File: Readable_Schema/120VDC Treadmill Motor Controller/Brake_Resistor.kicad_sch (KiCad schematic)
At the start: 13 parts, among them J7 TB005-762-02BE, Q9 IPP200N25N3GXKSA1, U10 FOD3182, U11 TC75S56F_LF

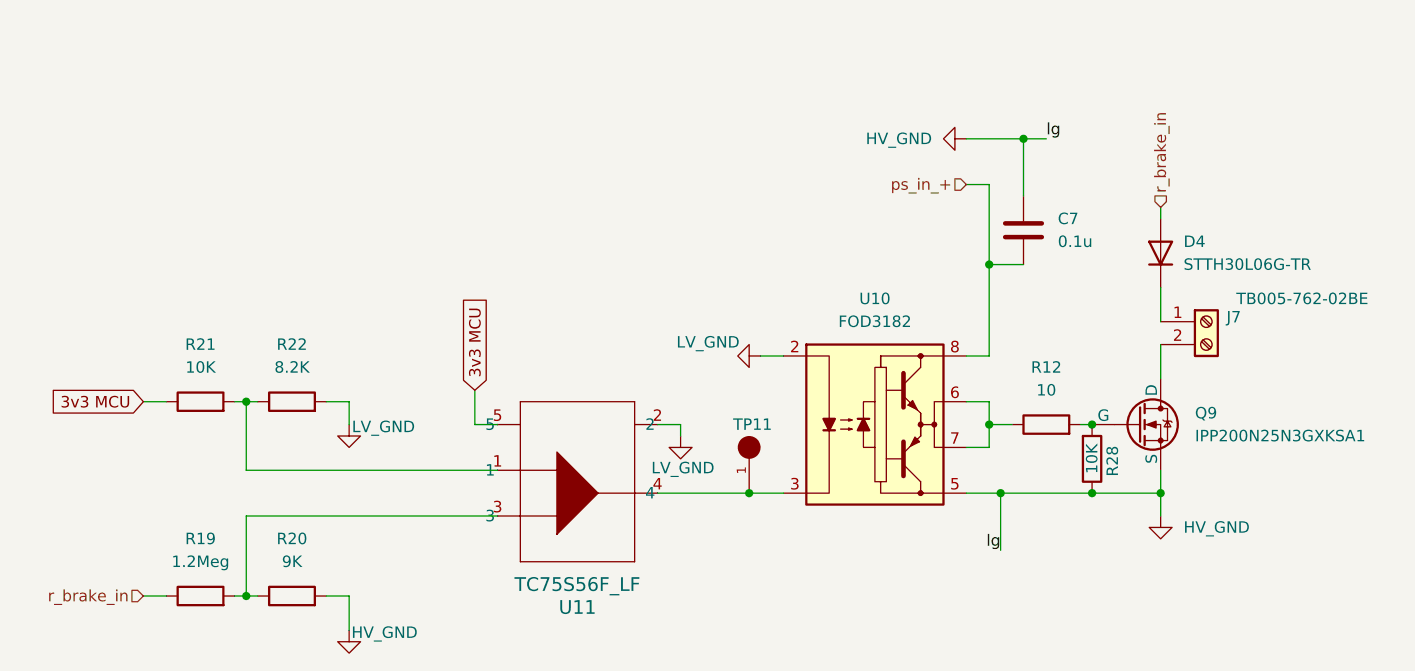
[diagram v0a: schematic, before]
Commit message: Reworking the whole comparator for brake resistor logic circuit as all my HV and LV grounds are messed up and I think the comparator I was using was wrong
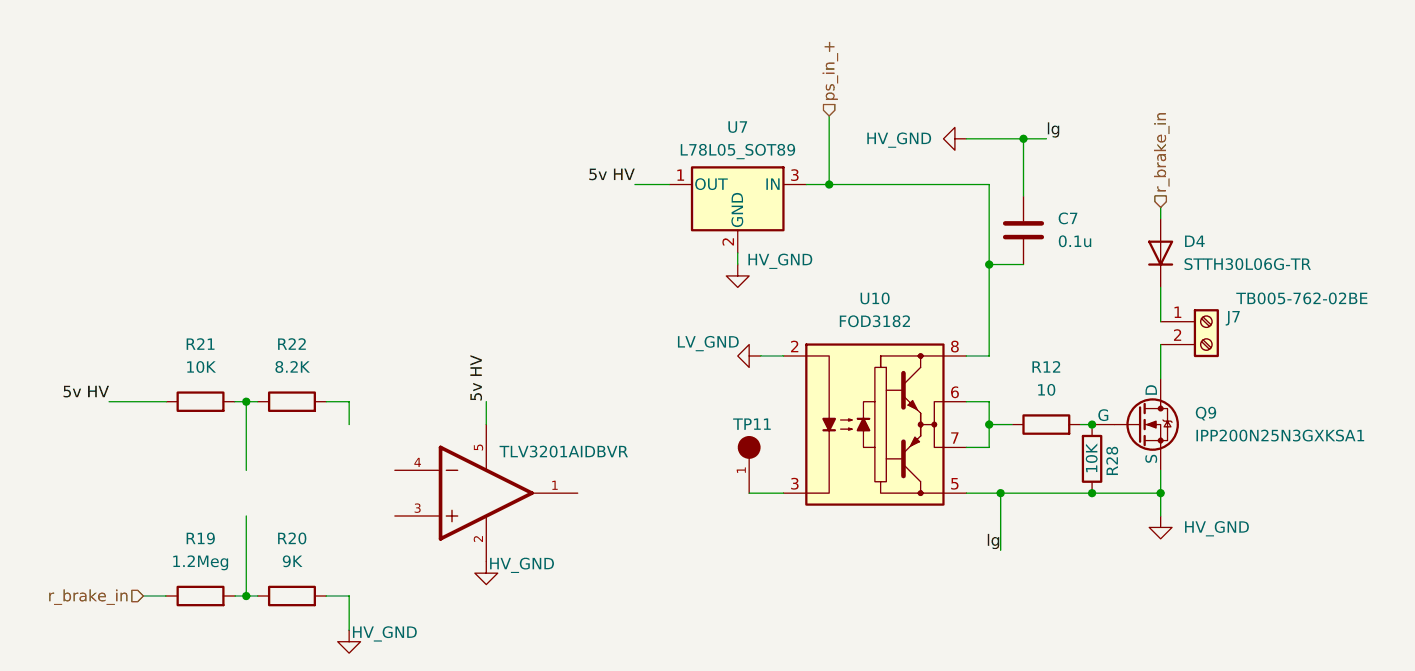
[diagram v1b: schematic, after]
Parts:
- removed U11: TC75S56F_LF, Treadmill_Feet:SOT-25 SMV_TOS, symbol Treadmill_Comp:TC75S56F_LF
- added U4: TLV3201AIDBVR, Treadmill_Feet:SOT95P280X145-5N, symbol Treadmill_Comp:TLV3201AIDBVR
- added U7: L78L05_SOT89, Package_TO_SOT_SMD:SOT-89-3, symbol Regulator_Linear:L78L05_SOT89
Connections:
- net HV_GND: now also U4.2, U7.2 (GND)
- net LV_GND: no longer R22.2
- net ps_in_+: now also U7.3 (IN)
- net 3v3 MCU renamed 5v HV
- net 5v HV: now also U4.5, U7.1 (OUT)

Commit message: -Tried to fix a decent portion of the feedback circuit. Basically the new gate drivers have a enable pin so it makes more sense to tie the OC pin directly to the function of EN. Also kept the SR latch as a method of delaying the restart and avoiding hysterysis -Still working through the brake resistor subcircuit, basically switching all comparator logic to HV and thinking of using optoisolation to feed comparator output to the gate driver to keep things isolated. Truthfully feels like I should just nuke that FOD3182 and use a bootstrap or something else since I could care less about isolation in that subcircuit since no communication with the microcontroller is needed.
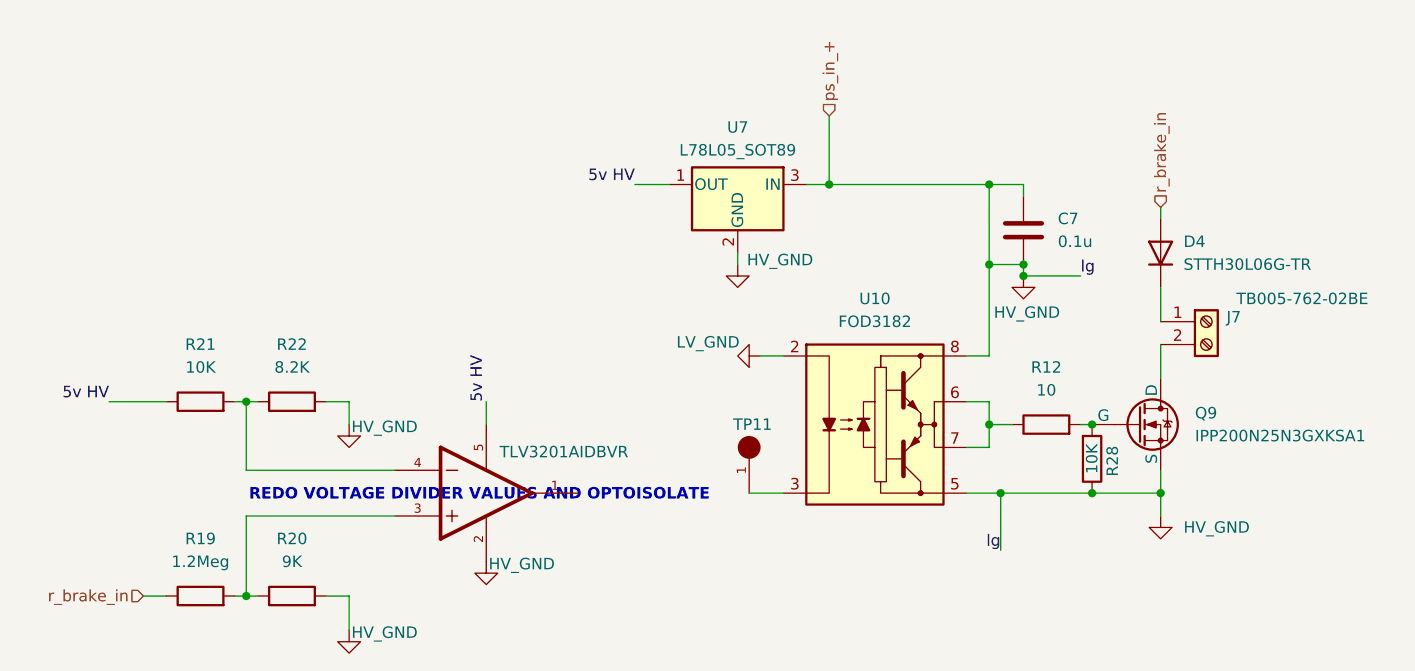
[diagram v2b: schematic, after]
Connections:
- net ps_in_+ is gone; now on net HV_GND: C7.2, U10.8 (VCC), U7.3 (IN)
- net HV_GND: now also R22.2
- net at U4.3: now also R19.2, R20.1
- net at U4.4: now also R21.2, R22.1
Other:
- note added: "REDO VOLTAGE DIVIDER VALUES AND OPTOISOLATE"
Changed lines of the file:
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@@
 	(generator_version "9.0")
 	(paper "A4")
+	(text "REDO VOLTAGE DIVIDER VALUES AND OPTOISOLATE"
+		(exclude_from_sim no)
+		(at 89.408 112.014 0)
+		(effects
+			(font
+				(size 1.27 1.27)
+				(thickness 0.254)
+				(bold yes)
+				(color 255 0 0 1)
+			)
+		)
+	)
 	(junction
 		(at 157.48 104.14)
@@
 	)
 	(junction
-		(at 157.48 111.76)
+		(at 149.86 86.36)
 		(diameter 0)
 		(color 0 0 0 0)
 	)
 	(junction
-		(at 149.86 72.39)
+		(at 157.48 111.76)
 		(diameter 0)
 		(color 0 0 0 0)
@@
 	)
 	(junction
+		(at 149.86 87.63)
+		(diameter 0)
+		(color 0 0 0 0)
+	)
+	(junction
 		(at 146.05 104.14)
 		(diameter 0)
 		(color 0 0 0 0)
 	)
+	(junction
+		(at 146.05 77.47)
+		(diameter 0)
+		(color 0 0 0 0)
+	)
 	(wire
 		(pts
@@
 	(wire
 		(pts
-			(xy 143.51 72.39) (xy 149.86 72.39)
-		)
-		(stroke
-			(width 0)
-			(type default)
-		)
-	)
-	(wire
-		(pts
 			(xy 63.5 114.3) (xy 63.5 123.19)
 		)
@@
 	(wire
 		(pts
+			(xy 149.86 78.74) (xy 149.86 77.47)
+		)
+		(stroke
+			(width 0)
+			(type default)
+		)
+	)
+	(wire
+		(pts
 			(xy 90.17 101.6) (xy 90.17 104.14)
 		)
@@
 	(wire
 		(pts
-			(xy 149.86 72.39) (xy 149.86 78.74)
+			(xy 63.5 114.3) (xy 80.01 114.3)
 		)
 		(stroke
@@
 	(wire
 		(pts
+			(xy 149.86 77.47) (xy 146.05 77.47)
+		)
+		(stroke
+			(width 0)
+			(type default)
+		)
+	)
+	(wire
+		(pts
 			(xy 118.11 85.09) (xy 118.11 86.36)
 		)
@@
 	(wire
 		(pts
+			(xy 149.86 87.63) (xy 156.21 87.63)
+		)
+		(stroke
+			(width 0)
+			(type default)
+		)
+	)
+	(wire
+		(pts
 			(xy 128.27 77.47) (xy 146.05 77.47)
 		)
@@
 	(wire
 		(pts
-			(xy 149.86 72.39) (xy 152.4 72.39)
+			(xy 149.86 86.36) (xy 149.86 87.63)
 		)
 		(stroke
@@
 		(pts
 			(xy 157.48 111.76) (xy 165.1 111.76)
+		)
+		(stroke
+			(width 0)
+			(type default)
+		)
+	)
+	(wire
+		(pts
+			(xy 63.5 109.22) (xy 80.01 109.22)
 		)
 		(stroke
@@
 	)
 	(label "lg"
-		(at 152.4 72.39 0)
+		(at 156.21 87.63 0)
 		(effects
 			(font
@@
 	(symbol
 		(lib_id "power:GND")
-		(at 143.51 72.39 270)
+		(at 149.86 87.63 0)
 		(unit 1)
 		(exclude_from_sim no)
@@
 		(dnp no)
 		(property "Reference" "#PWR026"
-			(at 137.16 72.39 0)
+			(at 149.86 93.98 0)
 			(effects
 				(font
@@
 		)
 		(property "Value" "HV_GND"
-			(at 139.7 72.3899 90)
+			(at 153.924 91.694 0)
 			(effects
 				(font
@@
 		)
 		(property "Footprint" ""
-			(at 143.51 72.39 0)
+			(at 149.86 87.63 0)
 			(effects
 				(font
@@
 		)
 		(property "Datasheet" ""
-			(at 143.51 72.39 0)
+			(at 149.86 87.63 0)
 			(effects
 				(font
@@
 		)
 		(property "Description" "Power symbol creates a global label with name \"GND\" , ground"
-			(at 143.51 72.39 0)
+			(at 149.86 87.63 0)
 			(effects
 				(font
@@
 					(unit 1)
 				)
+			)
+		)
+	)
+	(symbol
+		(lib_id "power:GND1")
+		(at 74.93 104.14 0)
+		(unit 1)
+		(exclude_from_sim no)
+		(in_bom yes)
+		(on_board yes)
+		(dnp no)
+		(property "Reference" "#PWR06"
+			(at 74.93 110.49 0)
+			(effects
+				(font
+					(size 1.27 1.27)
+				)
+				(hide yes)
+			)
+		)
+		(property "Value" "HV_GND"
+			(at 75.184 104.394 0)
+			(effects
+				(font
+					(size 1.27 1.27)
+				)
+				(justify left)
+			)
+		)
+		(property "Footprint" ""
+			(at 74.93 104.14 0)
+			(effects
+				(font
+					(size 1.27 1.27)
+				)
+				(hide yes)
+			)
+		)
+		(property "Datasheet" ""
+			(at 74.93 104.14 0)
+			(effects
+				(font
+					(size 1.27 1.27)
+				)
+				(hide yes)
+			)
+		)
+		(property "Description" "Power symbol creates a global label with name \"GND1\" , ground"
+			(at 74.93 104.14 0)
+			(effects
+				(font
+					(size 1.27 1.27)
+				)
+				(hide yes)
+			)
+		)
+		(pin "1"
+		)
+		(instances
+			(project "120VDC Treadmill Motor Controller"
+				(path "/319bc5c0-2dd5-4df3-a34b-9170833ebccd/7a7487b9-35f1-42d2-9ba5-cfe8e231a0f8"
+					(reference "#PWR06")
+					(unit 1)
+				)
